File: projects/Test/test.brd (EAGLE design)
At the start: 63.5 x 24.1 mm, 50 parts, among them J2 1755529, U1 STM32F405RGT6, U2 CSD88584Q5DCT, U3 CSD88584Q5DCT, U4 CSD88584Q5DCT, Y1 ECS-80-S-4X

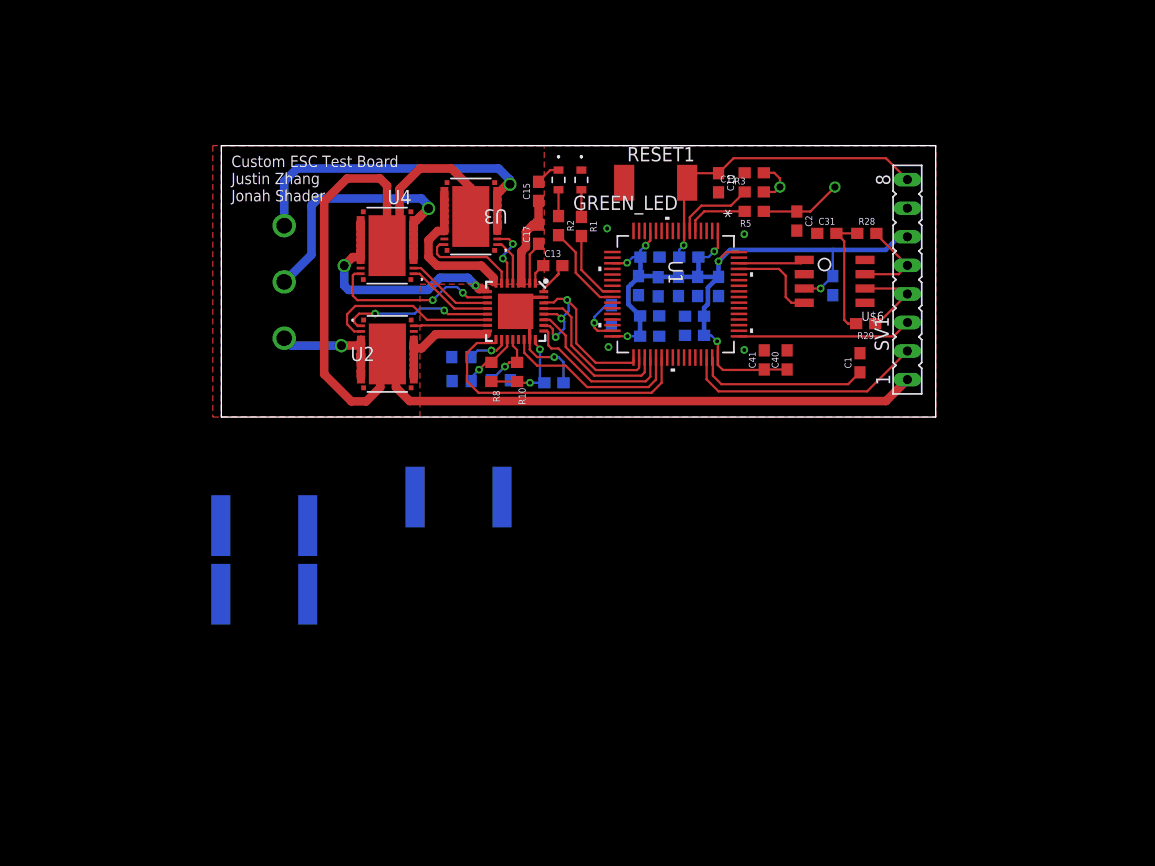
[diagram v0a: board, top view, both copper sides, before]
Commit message: Consolidate test boards to one place
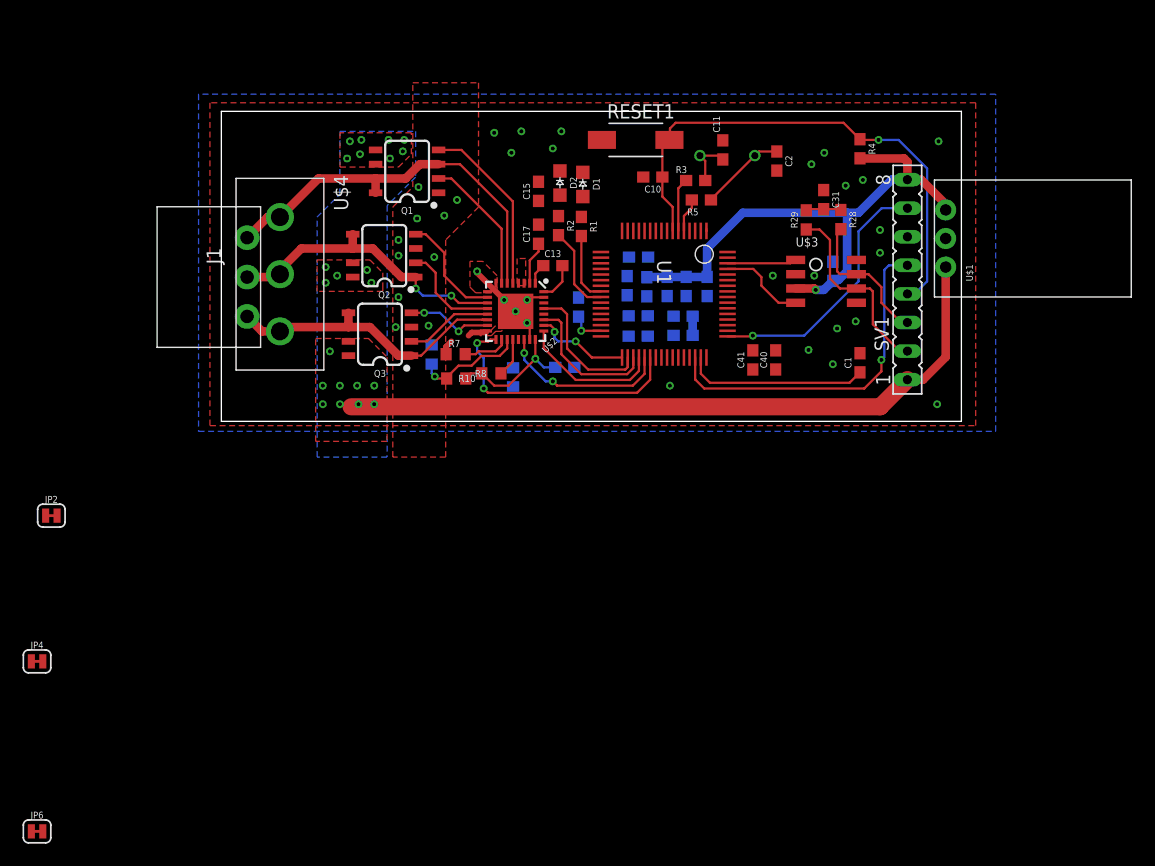
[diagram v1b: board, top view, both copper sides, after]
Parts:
- removed GREEN_LED, RED_LED: TLMS1100-GS08, VESC_SHIT:LED_VISHAY_TLMX1100
- removed J2: 1755529, VESC_SHIT:CONN_1755529
- removed R12, R13, R6: (no value), resistor-shunt:PMD
- removed U$6: TCAN337D, PI_Shield_Library:TCAN337D
- removed U2, U3, U4: CSD88584Q5DCT, VESC_SHIT:DMM0022A
- added D1: RED, LED-0805:0805
- added D2: GREEN, LED-0805:0805
- added J1: 284512-3, ThrusterConnector:284512-3
- added JP2, JP4, JP6: JUMPER-SMT_2_NC_TRACE_SILK, SparkFun-Jumpers:SMT-JUMPER_2_NC_TRACE_SILK
- added Q1, Q2, Q3: (no value), Dual NMOS:SO08
- added U$1: MURATA-DC-DC, MURATA_3pin_dcdc:MURATA-DC-DC
- added U$3: TCAN337D, STM and CAN parts:SOIC-8
- added U$4: 3PINCONNECTOR, afro_20A_esc:3PINCONNECTOR
- C10: value 4.7uF -> 0.1uF
- C11, C2: value 4.7uF -> 20pF
- C30: value 4.7uF -> 0.1IuF
- R1, R2: value 1k -> 470
- R3, R5: value 1k -> 0
- R4: value 1k -> 10k
- RESET1: device DiscreteComponents:SW_2512 -> Push button - FSM2JMTR:DISCRETECOMPONENTS_SW_2512
- U$2: device VESC_SHIT:QFN-32-5X5MM -> Motor Driver - DRV8320HRTVT:QFN-32-5X5MM
- U1: value STM32F405RGT6 -> (none); device VESC_SHIT:LQFP-64 -> STM32F405RGT6:LQFP-64
- moved R4 18.0 mm to (56.8, 23.9), flipped to the top, turned to 270 degrees
- moved R29 10.6 mm to (52.0, 17.5), turned to 90 degrees
- moved Y1 7.64 mm to (45.0, 23.2)
- moved C10 5.86 mm to (38.4, 21.3), turned to 180 degrees
- moved C2 5.62 mm to (49.4, 22.8)
- moved R3 5.31 mm to (42.2, 21.0)
- moved R5 4.81 mm to (42.7, 19.3)
- moved RESET1 4.20 mm to (36.8, 24.6)
- moved R9 3.56 mm to (18.7, 5.56), turned to 270 degrees
- moved C11 3.45 mm to (44.6, 23.7), turned to 90 degrees
- moved R8 3.18 mm to (20.9, 3.43), turned to 0 degrees
- moved C31 3.01 mm to (53.5, 19.3), turned to 270 degrees
- moved C3 3.00 mm to (31.8, 9.78), turned to 90 degrees
- moved R28 2.61 mm to (55.1, 17.6), turned to 270 degrees
- moved R10 2.29 mm to (24.0, 3.89), turned to 180 degrees
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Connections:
- net DVDD_1 renamed 3V3_OUT
- net N$1 renamed LED1
- net N$16 renamed CPL
- net N$17 renamed IDRIVE
- net N$18 renamed MODE
- net N$34 renamed V_CAP_L
- net N$4 renamed LED2
- net N$9 renamed CPH
- removed net INL_1: U$2.26, U$2.28, U$2.30, U1.33
- removed net N$2: GREEN_LED.2, R1.1
- removed net N$3: R2.1, RED_LED.2
- removed net SHA_1: U$2.6, U3.2
- removed net SHB_1: U$2.11, U4.2
- removed net SHC_1: U$2.14, U2.2
- removed net SLA_1: R6.1, U$2.8, U3.12, U3.13, U3.14, U3.15, U3.16, U3.17, U3.18, U3.19, U3.20
- removed net SLB_1: R12.1, U$2.9, U4.12, U4.13, U4.14, U4.15, U4.16, U4.17, U4.18, U4.19, U4.20
- removed net SLC_1: R13.1, U$2.16, U2.12, U2.13, U2.14, U2.15, U2.16, U2.17, U2.18, U2.19, U2.20
- new net DLA_1: JP2.1
- new net DLB_1: JP4.1
- new net DLC_1: JP6.1
- new net INLA_1: U$2.26, U1.33
- new net INLB_1: U$2.28
- new net INLC_1: U$2.30
- new net LED1_MID: D1.A, R1.1
- new net LED2_MID: D2.A, R2.1
- net 12V: now also Q1.5, Q1.6, Q2.7, Q2.8, Q3.7, Q3.8, U$1.1; no longer U2.27, U3.27, U4.27
- net 3V3: now also SV1.8, U$1.3, U$3.3; no longer SV1.6, U$6.VCC
- net CAN_H: now also SV1.3, U$3.7; no longer SV1.5, U$6.CANH
- net CAN_L: now also SV1.2, U$3.6; no longer SV1.4, U$6.CANL
- net CAN_RX: now also U$3.4; no longer U$6.RXD
- net CAN_TX: now also U$3.1; no longer U$6.TXD
- net GHA_1: now also Q1.4; no longer U3.1
- net GHB_1: now also Q2.2; no longer U4.1
- net GHC_1: now also Q3.2; no longer U2.1
- net GLA_1: now also Q1.2; no longer U3.22
- net GLB_1: now also Q2.4; no longer U4.22
- net GLC_1: now also Q3.4; no longer U2.22
- net GND: now also D1.C, D2.C, Q1.1, Q2.3, Q3.3, SV1.6, U$1.2, U$2.16, U$2.8, U$2.9, U$3.2; no longer GREEN_LED.1, R12.2, R13.2, R6.2, RED_LED.1, SV1.7, U$6.GND
- net NRST: now also SV1.4; no longer SV1.8
- net PHASE_A1: now also J1.3, JP2.2, Q1.3, Q1.7, Q1.8, U$2.6, U$4.A; no longer J2.1, U3.10, U3.11, U3.3, U3.4, U3.5, U3.6, U3.7, U3.8, U3.9
- net PHASE_B1: now also J1.2, JP4.2, Q2.1, Q2.5, Q2.6, U$2.11, U$4.B; no longer J2.2, U4.10, U4.11, U4.3, U4.4, U4.5, U4.6, U4.7, U4.8, U4.9
- net PHASE_C1: now also J1.1, JP6.2, Q3.1, Q3.5, Q3.6, U$2.14, U$4.C; no longer J2.3, U2.10, U2.11, U2.3, U2.4, U2.5, U2.6, U2.7, U2.8, U2.9
- net SWCLK: now also SV1.7; no longer SV1.3
- net SWDIO: now also SV1.5; no longer SV1.2
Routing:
- net 12V: track 111.8 -> 62.7 mm, vias 0 -> 22
- net SLB_1: track 22.9 -> 0.00 mm, vias 2 -> 0
- net INL_1: track 20.2 -> 0.00 mm, vias 3 -> 0
- net 3V3: track 71.3 -> 51.5 mm, vias 7 -> 1
- net NRST: track 28.2 -> 46.8 mm
- net SHC_1: track 15.7 -> 0.00 mm
- net SLA_1: track 15.2 -> 0.00 mm
- net SLC_1: track 12.8 -> 0.00 mm
- net PHASE_C1: track 14.2 -> 25.7 mm, vias 1 -> 0
- net GHA_1: track 4.24 -> 15.8 mm
- net CAN_L: track 7.92 -> 17.2 mm
- net SWDIO: track 21.7 -> 30.8 mm, vias 0 -> 1
- net INLA_1: track 0.00 -> 8.58 mm, vias 0 -> 2
- net N$46: track 11.0 -> 3.15 mm
- net SHB_1: track 7.86 -> 0.00 mm
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- added copper zone on layer 16, net 12V
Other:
- board size 63.5 x 24.1 mm -> 65.8 x 27.6 mm
- board text removed: "Custom ESC Test Board Justin Zhang Jonah Shader"

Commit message: Replace micro and driver. Remove CAN.
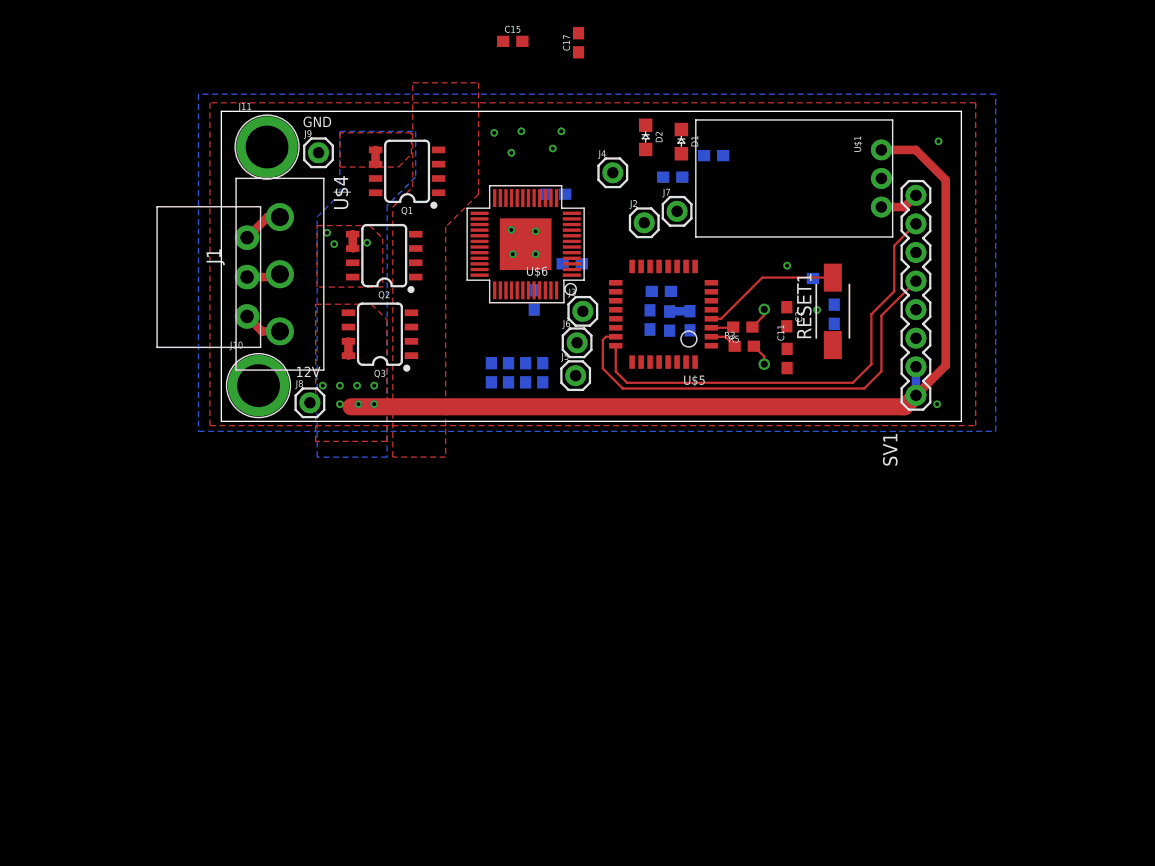
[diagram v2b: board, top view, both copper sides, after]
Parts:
- removed C1, C3: 2.2uF, SparkFun-Capacitors:0603
- removed C30: 0.1IuF, SparkFun-Capacitors:0603
- removed C31: 0.1uF, SparkFun-Capacitors:0603
- removed C32, C33, C34, C35, C4, C40, C41, C5: 4.7uF, SparkFun-Capacitors:0603
- removed JP2, JP4, JP6: JUMPER-SMT_2_NC_TRACE_SILK, SparkFun-Jumpers:SMT-JUMPER_2_NC_TRACE_SILK
- removed R28, R29: 60, SparkFun-Resistors:0603
- removed U$2: DRV8320H, Motor Driver - DRV8320HRTVT:QFN-32-5X5MM
- removed U$3: TCAN337D, STM and CAN parts:SOIC-8
- removed U1: (no value), STM32F405RGT6:LQFP-64
- added J10, J11: (no value), SparkFun-Connectors:BANANA_CONN
- added J2, J3, J4, J5, J6, J7, J8, J9: (no value), SparkFun-Connectors:1X01
- added U$5: STM32F042K6T6, STM and CAN parts:LQFP32
- added U$6: DRV8340H, Motor Driver - DRV8340H:48-TQFP
- C16, C38, C39: value 4.7uF -> 0.1uF
- R1, R2: value 470 -> 1k
- R10, R11, R8, R9: value (none) -> (none); device rcl:R0603 -> SparkFun-Resistors:0603
- R4: value 10k -> 1k
- R7: device rcl:R0603 -> SparkFun-Resistors:0603
- SV1: device con-lsta:FE08 -> SparkFun-Connectors:1X08
- moved RESET1 23.2 mm to (54.4, 9.40), turned to 90 degrees
- moved C10 20.2 mm to (54.5, 9.14), flipped to the bottom, turned to 270 degrees
- moved C11 19.4 mm to (50.3, 5.21)
- moved C17 17.4 mm to (31.8, 33.3)
- moved Y1 16.4 mm to (48.3, 7.14), turned to 270 degrees
- moved R3 15.4 mm to (46.5, 6.30)
- moved C2 13.9 mm to (50.3, 8.92)
- moved C15 13.5 mm to (25.9, 33.4), turned to 0 degrees
- moved R1 13.3 mm to (43.8, 23.2), flipped to the bottom, turned to 180 degrees
- moved R4 12.0 mm to (53.4, 12.3), flipped to the bottom, turned to 0 degrees
- moved R5 11.9 mm to (46.4, 8.00)
- moved R2 11.0 mm to (40.1, 21.3), flipped to the bottom, turned to 180 degrees
- moved SV1 10.3 mm to (61.7, 1.93)
- moved D1 9.56 mm to (40.9, 24.5)
- moved C14 9.22 mm to (31.2, 13.6), turned to 0 degrees
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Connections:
- net N$7 renamed OSC_XTAL_2
- net N$8 renamed OSC_XTAL_1
- removed net CAN_H: R28.2, SV1.3, U$3.7
- removed net CAN_L: R29.1, SV1.2, U$3.6
- removed net CAN_RX: U$3.4, U1.61
- removed net CAN_TX: U$3.1, U1.62
- removed net DLA_1: JP2.1
- removed net DLB_1: JP4.1
- removed net DLC_1: JP6.1
- removed net INL_2: U1.39
- removed net N$19: R10.1, R11.2, U$2.20
- removed net N$46: C31.2, R28.1, R29.2
- removed net N$5: C1.1, U1.47
- removed net N$6: C3.1, U1.31
- new net +3V3: C12.1, C16.1, C38.1, C39.1, R4.2, U$5.1, U$5.17, U$5.5
- new net N$1: U$5.26, U$5.27, U$5.28, U$5.29
- new net VDS: R10.1, R11.2, U$6.34
- net 12V: now also J10.P$1, J8.1, Q1.7, Q1.8, Q3.5, Q3.6, SV1.2, U$6.4, U$6.5; no longer Q1.5, Q1.6, Q3.7, Q3.8, U$2.3, U$2.4
- net 3V3: no longer C12.1, C16.1, C30.1, C32.1, C33.1, C34.1, C35.1, C38.1, C39.1, C4.1, C40.1, C41.1, C5.1, R4.2, U$3.3, U1.1, U1.13, U1.19, U1.32, U1.48, U1.64
- net 3V3_OUT: now also U$6.39; no longer U$2.24
- net CPH: now also U$6.2; no longer U$2.1
- net CPL: now also U$6.1; no longer U$2.32
- net EN_1: now also U$5.21, U$6.36; no longer U$2.22, U1.37
- net FAULT_1: now also U$5.22, U$6.31; no longer U$2.17, U1.38
- net GHA_1: now also Q1.2, U$6.6; no longer Q1.4, U$2.5
- net GHB_1: now also U$6.19; no longer U$2.12
- net GHC_1: now also Q3.4, U$6.20; no longer Q3.2, U$2.13
- net GLA_1: now also Q1.4, U$6.9; no longer Q1.2, U$2.7
- net GLB_1: now also U$6.16; no longer U$2.10
- net GLC_1: now also Q3.2, U$6.23; no longer Q3.4, U$2.15
- net GND: now also J11.P$1, J9.1, Q1.3, Q3.1, SV1.3, U$5.16, U$5.31, U$5.32, U$6.10, U$6.11, U$6.12, U$6.13, U$6.14, U$6.15, U$6.24, U$6.25, U$6.26, U$6.27, U$6.28, U$6.29, U$6.30, U$6.37, U$6.38, U$6.47, U$6.48, U$6.PAD; no longer C1.2, C3.2, C30.2, C31.1, C32.2, C33.2, C34.2, C35.2, C4.2, C40.2, C41.2, C5.2, Q1.1, Q3.3, U$2.16, U$2.23, U$2.31, U$2.8, U$2.9, U$2.EP, U$3.2, U1.12, U1.18, U1.60, U1.63
- net IDRIVE: now also U$6.33; no longer U$2.19
- net INHA_1: now also J2.1, U$5.12, U$6.41; no longer U$2.25, U1.36
- net INHB_1: now also J3.1, U$5.19, U$6.43; no longer U$2.27, U1.35
- net INHC_1: now also J4.1, U$5.13, U$6.45; no longer U$2.29, U1.34
- net INLA_1: now also J5.1, U$5.18, U$6.42; no longer U$2.26, U1.33
- net INLB_1: now also J6.1, U$5.20, U$6.44; no longer U$2.28
- net INLC_1: now also J7.1, U$5.10, U$6.46; no longer U$2.30
- net LED1: now also U$5.6; no longer U1.24
- net LED2: now also U$5.7; no longer U1.25
- net MODE: now also U$6.32; no longer U$2.18
- net NRST: now also U$5.4; no longer U1.7
- net OSC_IN: now also U$5.3; no longer U1.5
- net OSC_OUT: now also U$5.2; no longer U1.6
- net PHASE_A1: now also Q1.1, Q1.5, Q1.6, U$6.7, U$6.8; no longer JP2.2, Q1.3, Q1.7, Q1.8, U$2.6
- net PHASE_B1: now also U$6.17, U$6.18; no longer JP4.2, U$2.11
- net PHASE_C1: now also Q3.3, Q3.7, Q3.8, U$6.21, U$6.22; no longer JP6.2, Q3.1, Q3.5, Q3.6, U$2.14
- net SWCLK: now also U$5.24; no longer U1.49
- net SWDIO: now also U$5.23; no longer U1.46
- net V_CAP_L: now also U$6.3; no longer U$2.2
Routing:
- net 3V3: track 51.5 -> 3.50 mm, vias 1 -> 0
- net NRST: track 46.8 -> 12.3 mm, vias 1 -> 0
- net PHASE_A1: track 35.2 -> 4.95 mm
- net FAULT_1: track 23.5 -> 0.00 mm, vias 2 -> 0
- net PHASE_B1: track 26.5 -> 4.30 mm, vias 2 -> 0
- net PHASE_C1: track 25.7 -> 4.74 mm
- net 12V: track 62.7 -> 80.2 mm, vias 22 -> 10
- net CAN_L: track 17.2 -> 0.00 mm
- net SWCLK: track 23.3 -> 40.2 mm, vias 1 -> 0
- net N$5: track 16.3 -> 0.00 mm
- net GHA_1: track 15.8 -> 0.00 mm
- net EN_1: track 15.4 -> 0.00 mm, vias 2 -> 0
- net GND: track 14.7 -> 0.00 mm, vias 35 -> 13
- net CAN_H: track 12.8 -> 0.00 mm
- net INHB_1: track 12.8 -> 0.00 mm
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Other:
- board text added: "12V"
- board text added: "GND"

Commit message: Add motor driver bottom pad and breakout can rx/tx pins
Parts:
- added J12: (no value), SparkFun-Connectors:1X02
- U$6: value DRV8340H -> DRV8340HBOTTOM-PAD; device Motor Driver - DRV8340H:48-TQFP -> Motor Driver - DRV8340H:48-TQFP-BOTTOM
- moved C10 1.45 mm to (54.1, 10.5)
- moved C11 1.45 mm to (49.9, 6.60)
- moved C12 1.45 mm to (39.5, 9.93)
- moved C16 1.45 mm to (38.7, 12.6)
- moved C2 1.45 mm to (49.9, 10.3)
- moved C38 1.45 mm to (41.3, 9.96)
- moved C39 1.45 mm to (37.7, 10.0)
- moved R3 1.45 mm to (46.1, 7.70)
- moved R5 1.45 mm to (46.0, 9.40)
- moved RESET1 1.45 mm to (54.0, 10.8)
- moved U$5 1.45 mm to (43.2, 13.3)
- moved Y1 1.45 mm to (47.9, 8.53)
- moved R4 1.45 mm to (53.1, 13.7)
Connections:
- new net CAN_RX: J12.2, U$5.21
- new net CAN_TX: J12.1, U$5.22
- net 12V: now also Q1.5, Q1.6; no longer Q1.7, Q1.8
- net EN_1: now also U$5.25; no longer U$5.21
- net FAULT_1: now also U$5.26; no longer U$5.22
- net GHA_1: now also Q1.4; no longer Q1.2
- net GLA_1: now also Q1.2; no longer Q1.4
- net GND: now also Q1.1, U$6.PAD_BOT; no longer Q1.3
- net N$1: no longer U$5.26, U$5.27
- net PHASE_A1: now also Q1.3, Q1.7, Q1.8; no longer Q1.1, Q1.5, Q1.6
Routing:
- net PHASE_A1: track 4.95 -> 1.27 mm
- net SWCLK: track 40.2 -> 43.8 mm
- net PHASE_C1: track 4.74 -> 1.27 mm
- net SWDIO: track 39.2 -> 42.6 mm
- net PHASE_B1: track 4.30 -> 1.27 mm
